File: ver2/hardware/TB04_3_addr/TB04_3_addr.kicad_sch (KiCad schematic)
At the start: 12 parts, among them J101 USB_C_Receptacle_PowerOnly_6P, SW101 SW_SPDT, U101 74LS157, U102 74HC138

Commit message: ver2: アドレス基板を分割し4枚すべて完了(要修正1件)
TB04_3_addr を分割。45部品・56信号すべてバスへ引き出し済み。
署名が変わったのは J101 のみ(USB-C→バスヘッダ)。
旧トップシート TB04addr8bit.kicad_sch も削除。

要修正: 3_addr の J103 で INPUT/OUTPUT のビット順が 4_io と逆
(pin25=INPUT0 になっている。正は pin25=INPUT3)

Co-Authored-By: Claude Opus 5 <noreply@anthropic.com>
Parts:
- removed C101, C102: 0.1u, Capacitor_THT:C_Disc_D4.3mm_W1.9mm_P5.00mm, symbol Device:C
- removed J101: USB_C_Receptacle_PowerOnly_6P, Library:USB_C_receptacle_onlypower_tanuki, symbol New_Library:USB_C_Receptacle_PowerOnly_6P_tanuki
- removed R101, R102: 5.1K, Resistor_THT:R_Axial_DIN0207_L6.3mm_D2.5mm_P10.16mm_Horizontal, symbol Device:R
- removed SW101: SW_SPDT, Library:sw_slide, symbol Switch:SW_SPDT
- removed U101: 74LS157, symbol 74xx:74LS157
- removed U102: 74HC138, Package_DIP:DIP-16_W7.62mm_Socket, symbol 74xx:74HC138
- added J101, J102, J103: Conn_02x20_Odd_Even, symbol Connector_Generic:Conn_02x20_Odd_Even
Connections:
- net EXE: now also J101.3 (Pin_3)
- net GND: now also J101.10 (Pin_10), J101.12 (Pin_12), J101.14 (Pin_14), J101.16 (Pin_16), J101.18 (Pin_18), J101.2 (Pin_2), J101.20 (Pin_20), J101.22 (Pin_22), J101.24 (Pin_24), J101.26 (Pin_26), J101.28 (Pin_28), J101.30 (Pin_30), J101.32 (Pin_32), J101.34 (Pin_34), J101.36 (Pin_36), J101.4 (Pin_4), J101.6 (Pin_6), J101.8 (Pin_8), J102.2 (Pin_2), J102.21 (Pin_21), J102.23 (Pin_23), J102.26 (Pin_26), J102.28 (Pin_28), J102.30 (Pin_30), J102.32 (Pin_32), J102.34 (Pin_34), J102.36 (Pin_36), J102.38 (Pin_38), J102.4 (Pin_4), J102.40 (Pin_40), J103.2 (Pin_2), J103.21 (Pin_21), J103.23 (Pin_23), J103.26 (Pin_26), J103.28 (Pin_28), J103.30 (Pin_30), J103.32 (Pin_32), J103.34 (Pin_34), J103.36 (Pin_36), J103.38 (Pin_38), J103.4 (Pin_4), J103.40 (Pin_40)
- net OPR10: now also J102.13 (Pin_13)
- net OPR4: now also J102.7 (Pin_7)
- net OPR5: now also J102.8 (Pin_8)
- net OPR6: now also J102.9 (Pin_9)
- net OPR8: now also J102.11 (Pin_11)
- net OPR9: now also J102.12 (Pin_12)
- net VDD: now also J101.38 (Pin_38), J101.40 (Pin_40)
- new net A0: J101.23 (Pin_23)
- new net A1: J101.21 (Pin_21)
- new net A2: J101.19 (Pin_19)
- new net A3: J101.17 (Pin_17)
- new net A4: J101.15 (Pin_15)
- new net A5: J101.13 (Pin_13)
- new net A6: J101.11 (Pin_11)
- new net A7: J101.9 (Pin_9)
- new net CD: J103.1 (Pin_1)
- new net CLK_CPU: J101.1 (Pin_1)
- new net CU: J103.3 (Pin_3)
- new net INPUT0: J103.25 (Pin_25)
- new net INPUT1: J103.27 (Pin_27)
- new net INPUT2: J103.29 (Pin_29)
- new net INPUT3: J103.31 (Pin_31)
- new net MD0: J101.39 (Pin_39)
- new net MD1: J101.37 (Pin_37)
- new net MD2: J101.35 (Pin_35)
- new net MD3: J101.33 (Pin_33)
- new net MD4: J101.31 (Pin_31)
- new net MD5: J101.29 (Pin_29)
- new net MD6: J101.27 (Pin_27)
- new net MD7: J101.25 (Pin_25)
- new net OPR11: J102.14 (Pin_14)
- new net OPR7: J102.10 (Pin_10)
- new net OUTPUT0: J103.33 (Pin_33)
- new net OUTPUT1: J103.35 (Pin_35)
- new net OUTPUT2: J103.37 (Pin_37)
- new net OUTPUT3: J103.39 (Pin_39)
- new net PC_CNT_EN: J103.5 (Pin_5)
- new net SEL_IMM: J102.24 (Pin_24)
- new net SEL_M0: J103.13 (Pin_13)
- new net SEL_M1: J103.14 (Pin_14)
- new net SEL_PC: J103.15 (Pin_15)
- new net SP0: J103.16 (Pin_16)
- new net SP1: J103.17 (Pin_17)
- new net SP2: J103.18 (Pin_18)
- new net YD0: J103.19 (Pin_19)
- new net YD1: J103.20 (Pin_20)
- new net YD2: J103.22 (Pin_22)
- new net YD3: J103.24 (Pin_24)
- new net ~{CS_RAM}: J103.7 (Pin_7)
- new net ~{OE_RAM}: J103.8 (Pin_8)
- new net ~{OE_ioAddr}: J103.9 (Pin_9)
- new net ~{PC_PE}: J103.6 (Pin_6)
- new net ~{RST}: J101.7 (Pin_7)
- new net ~{WE_RAM}: J103.10 (Pin_10)
- new net ~{YEN_PC}: J103.11 (Pin_11)
- new net ~{YEN_Y}: J103.12 (Pin_12)
- no-connect marks 6 -> 20
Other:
- removed sheet CLK_RST
- removed sheet Decoder
- removed sheet ROM_ALU
- removed sheet RS00
- removed sheet RS01
- removed sheet addrDecord
- removed sheet gates
- removed sheet inPort
- removed sheet outPort
- moved on the sheet: C103, C104, D101, R103

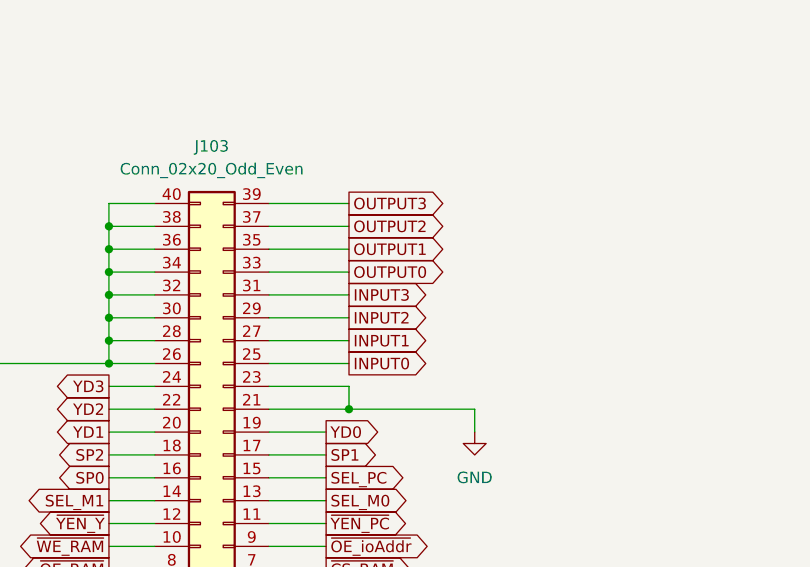
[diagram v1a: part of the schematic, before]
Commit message: ver2: 3_addrのINPUT/OUTPUTのビット順を修正し4枚の整合が取れた
120ピン全数の突合で不一致0。基板4分割が完了。

Co-Authored-By: Claude Opus 5 <noreply@anthropic.com>
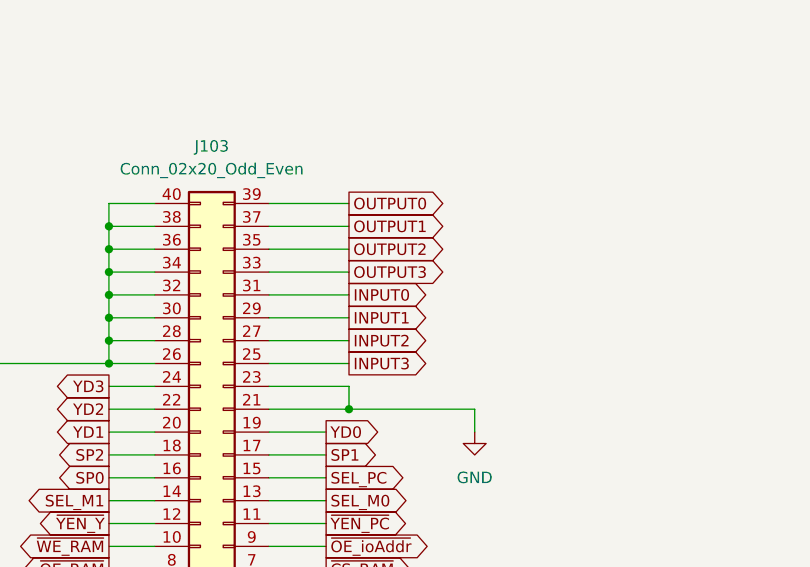
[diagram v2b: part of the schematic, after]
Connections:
- net INPUT0: now also J103.31 (Pin_31); no longer J103.25 (Pin_25)
- net INPUT1: now also J103.29 (Pin_29); no longer J103.27 (Pin_27)
- net INPUT2: now also J103.27 (Pin_27); no longer J103.29 (Pin_29)
- net INPUT3: now also J103.25 (Pin_25); no longer J103.31 (Pin_31)
- net OUTPUT0: now also J103.39 (Pin_39); no longer J103.33 (Pin_33)
- net OUTPUT1: now also J103.37 (Pin_37); no longer J103.35 (Pin_35)
- net OUTPUT2: now also J103.35 (Pin_35); no longer J103.37 (Pin_37)
- net OUTPUT3: now also J103.33 (Pin_33); no longer J103.39 (Pin_39)
